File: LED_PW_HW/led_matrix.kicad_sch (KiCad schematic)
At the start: 145 parts

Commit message: imported first footprints to pcb to get an idea
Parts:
- D1, D10, D100, D101, D102, D103, D104, D105, D106, D107, D108, D109, D11, D110, D111, D112, D113, D114, D115, D116, D117, D118, D119, D12, D120, D121, D122, D123, D124, D125, D126, D127, D128, D129, D13, D130, D131, D132, D133, D134, D135, D136, D137, D138, D139, D14, D140, D141, D142, D143, D144, D15, D16, D17, D18, D19, D2, D20, D21, D22, D23, D24, D25, D26, D27, D28, D29, D3, D30, D31, D32, D33, D34, D35, D36, D37, D38, D39, D4, D40, D41, D42, D43, D44, D45, D46, D47, D48, D49, D5, D50, D51, D52, D53, D54, D55, D56, D57, D58, D59, D6, D60, D61, D62, D63, D64, D65, D66, D67, D68, D69, D7, D70, D71, D72, D73, D74, D75, D76, D77, D78, D79, D8, D80, D81, D82, D83, D84, D85, D86, D87, D88, D89, D9, D90, D91, D92, D93, D94, D95, D96, D97, D98, D99: renamed from D?; footprint (none) -> LED_SMD:LED_0201_0603Metric_Pad0.64x0.40mm_HandSolder
- U1: renamed from U?; footprint (none) -> LED_PW_HW_Library:IS31FL3732A

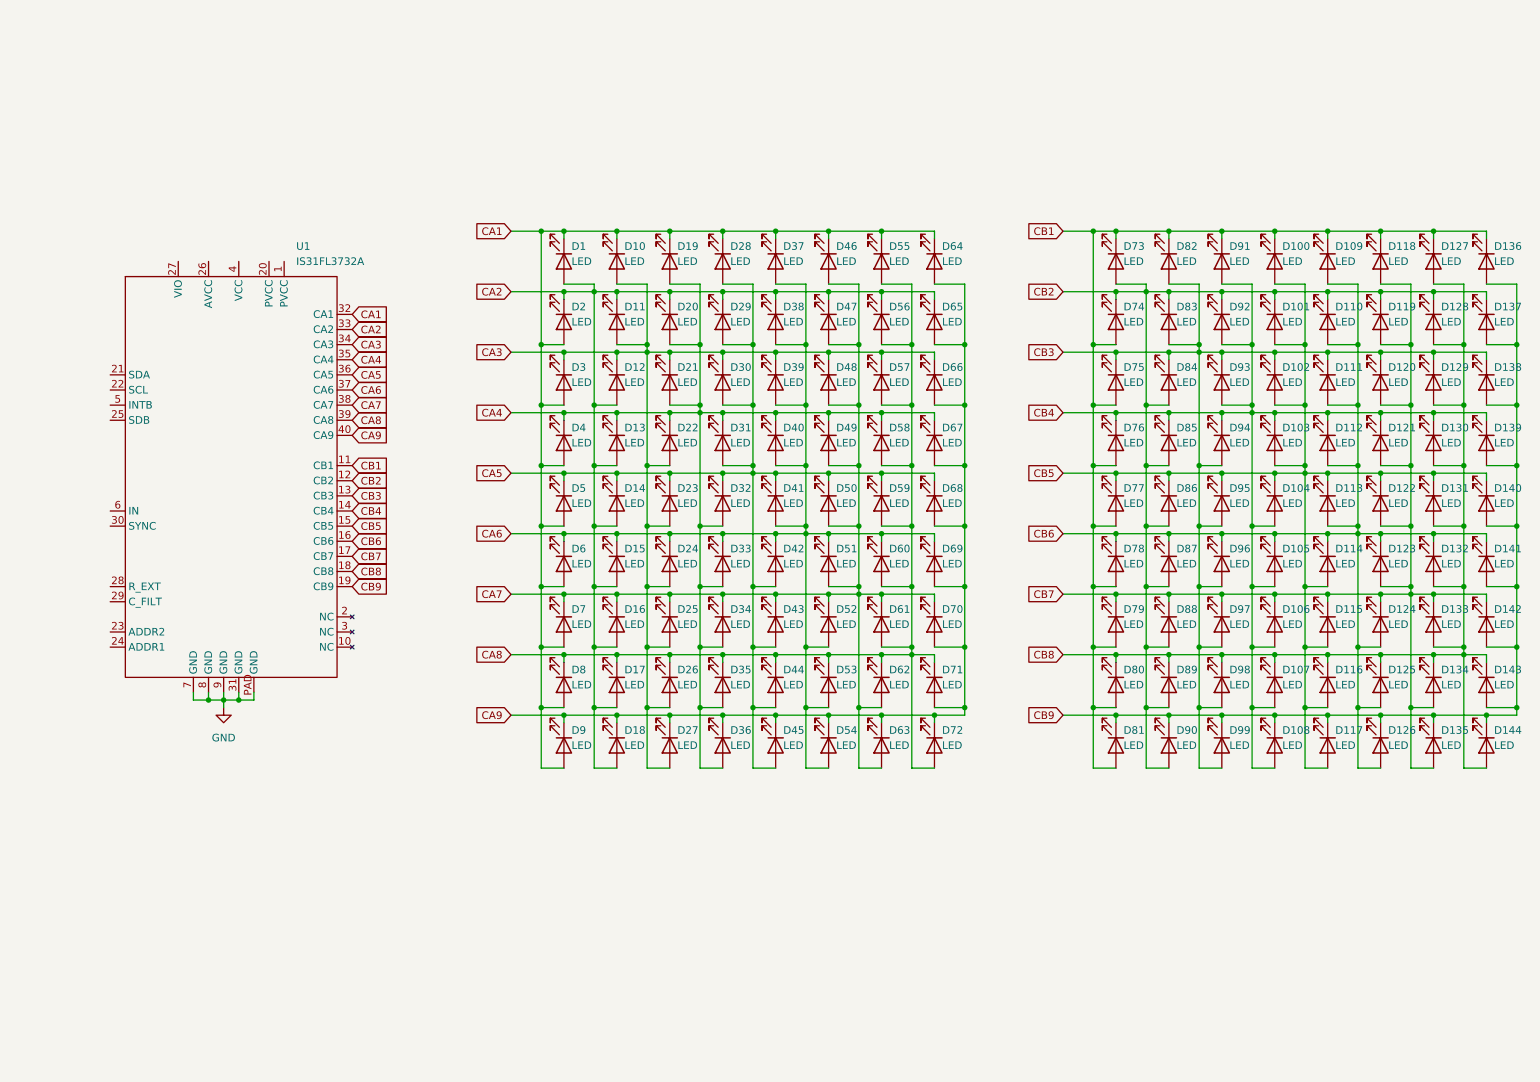
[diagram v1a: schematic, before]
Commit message: schematic of led driver part done
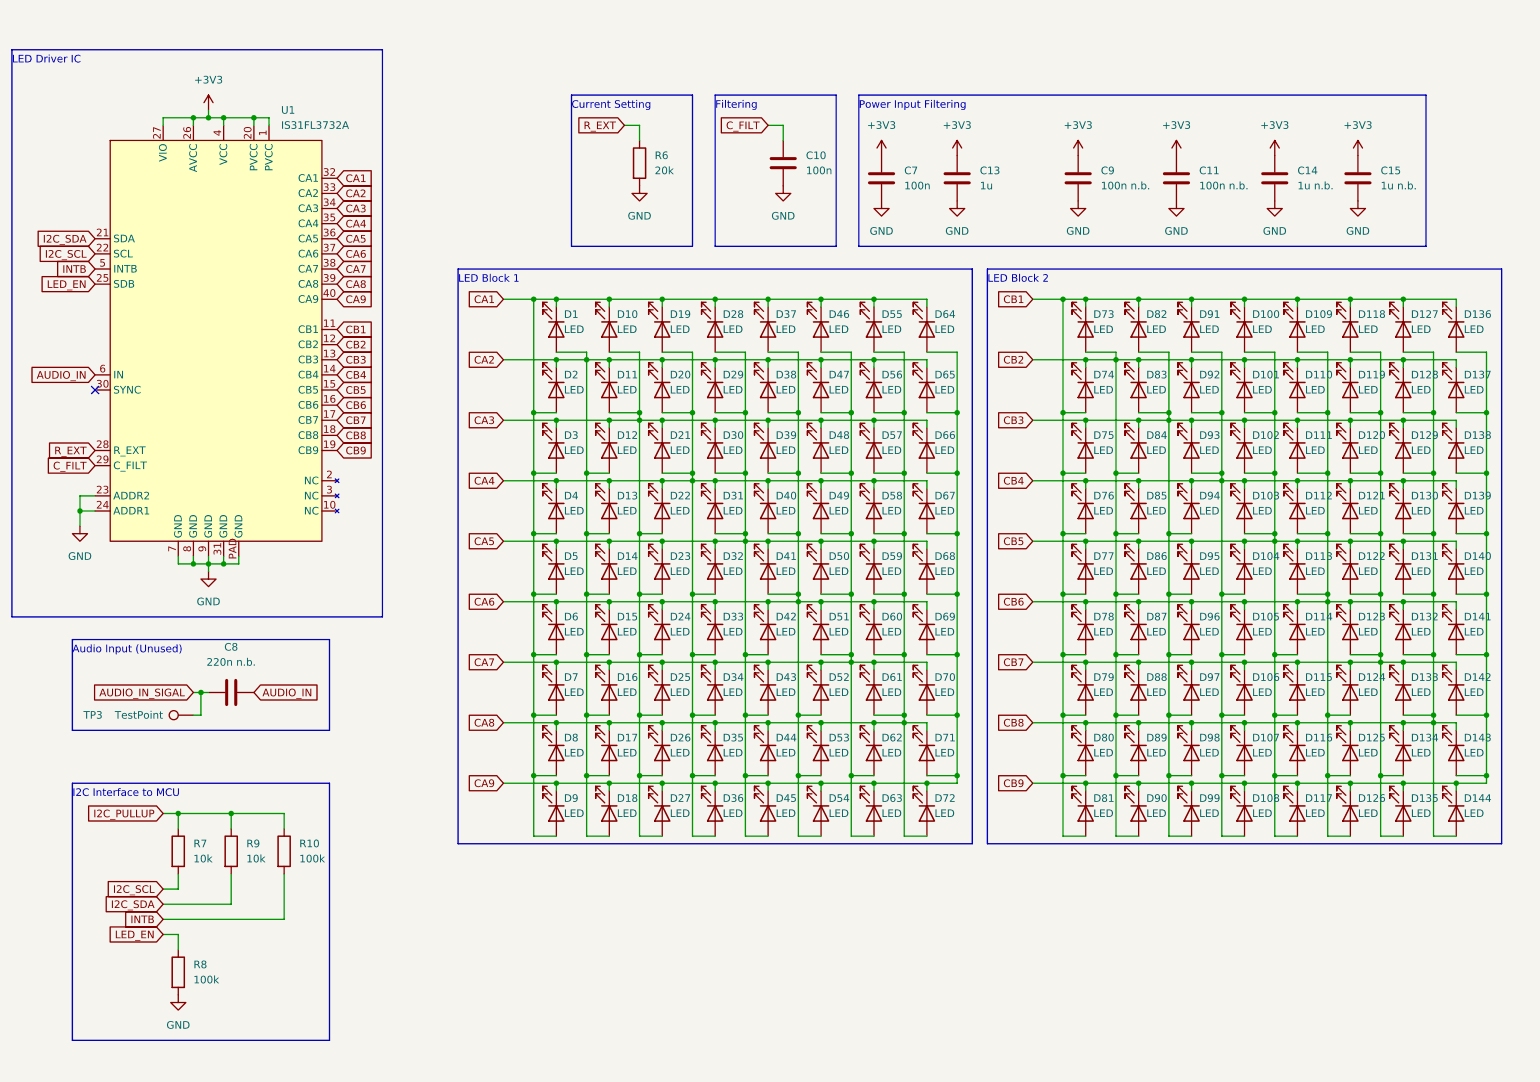
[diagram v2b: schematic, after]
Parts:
- added C10, C7: 100n, Capacitor_SMD:C_0603_1608Metric_Pad1.08x0.95mm_HandSolder, symbol Device:C
- added C11, C9: 100n n.b., Capacitor_SMD:C_0603_1608Metric_Pad1.08x0.95mm_HandSolder, symbol Device:C
- added C13: 1u, Capacitor_SMD:C_0603_1608Metric_Pad1.08x0.95mm_HandSolder, symbol Device:C
- added C14, C15: 1u n.b., Capacitor_SMD:C_0603_1608Metric_Pad1.08x0.95mm_HandSolder, symbol Device:C
- added C8: 220n n.b., Capacitor_SMD:C_0603_1608Metric_Pad1.08x0.95mm_HandSolder, symbol Device:C
- added R10, R8: 100k, Resistor_SMD:R_0603_1608Metric_Pad0.98x0.95mm_HandSolder, symbol Device:R
- added R6: 20k, Resistor_SMD:R_0603_1608Metric_Pad0.98x0.95mm_HandSolder, symbol Device:R
- added R7, R9: 10k, Resistor_SMD:R_0603_1608Metric_Pad0.98x0.95mm_HandSolder, symbol Device:R
- added TP3: TestPoint, TestPoint:TestPoint_Pad_D1.5mm, symbol Connector:TestPoint
- D1, D10, D100, D101, D102, D103, D104, D105, D106, D107, D108, D109, D11, D110, D111, D112, D113, D114, D115, D116, D117, D118, D119, D12, D120, D121, D122, D123, D124, D125, D126, D127, D128, D129, D13, D130, D131, D132, D133, D134, D135, D136, D137, D138, D139, D14, D140, D141, D142, D143, D144, D15, D16, D17, D18, D19, D2, D20, D21, D22, D23, D24, D25, D26, D27, D28, D29, D3, D30, D31, D32, D33, D34, D35, D36, D37, D38, D39, D4, D40, D41, D42, D43, D44, D45, D46, D47, D48, D49, D5, D50, D51, D52, D53, D54, D55, D56, D57, D58, D59, D6, D60, D61, D62, D63, D64, D65, D66, D67, D68, D69, D7, D70, D71, D72, D73, D74, D75, D76, D77, D78, D79, D8, D80, D81, D82, D83, D84, D85, D86, D87, D88, D89, D9, D90, D91, D92, D93, D94, D95, D96, D97, D98, D99: footprint LED_SMD:LED_0201_0603Metric_Pad0.64x0.40mm_HandSolder -> LED_SMD:LED_0603_1608Metric_Pad1.05x0.95mm_HandSolder
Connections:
- net GND: now also U1.23 (ADDR2), U1.24 (ADDR1), C10.2, C11.2, C13.2, C14.2, C15.2, C7.2, C9.2, R6.2, R8.2
- net +3V3: now reaches U1.1 (PVCC)
- net +3V3: now also U1.20 (PVCC), U1.26 (AVCC), U1.27 (VIO), U1.4 (VCC), C11.1, C13.1, C14.1, C15.1, C7.1, C9.1
- net I2C_SDA: now reaches U1.21 (SDA)
- net I2C_SDA: now also R9.2
- net I2C_SCL: now reaches U1.22 (SCL)
- net I2C_SCL: now also R7.2
- net LED_EN: now reaches U1.25 (SDB)
- net LED_EN: now also R8.1
- net R_EXT: now reaches U1.28 (R_EXT)
- net R_EXT: now also R6.1
- net C_FILT: now reaches U1.29 (C_FILT)
- net C_FILT: now also C10.1
- net INTB: now reaches U1.5 (INTB)
- net INTB: now also R10.2
- net AUDIO_IN: now reaches U1.6 (IN)
- net AUDIO_IN: now also C8.1
- new net AUDIO_IN_SIGAL: C8.2, TP3.1
- new net I2C_PULLUP: R10.1, R7.1, R9.1
- no-connect marks 0 -> 1
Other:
- note added: "Audio Input (Unused)"
- note added: "Current Setting"
- note added: "Filtering"
- note added: "I2C Interface to MCU"
- note added: "LED Block 1"
- note added: "LED Block 2"
- note added: "LED Driver IC"
- note added: "Power Input Filtering"
- moved on the sheet: D1, D10, D100, D101, D102, D103, D104, D105, D106, D107, D108, D109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

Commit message: giving up for now and going with 72 leds
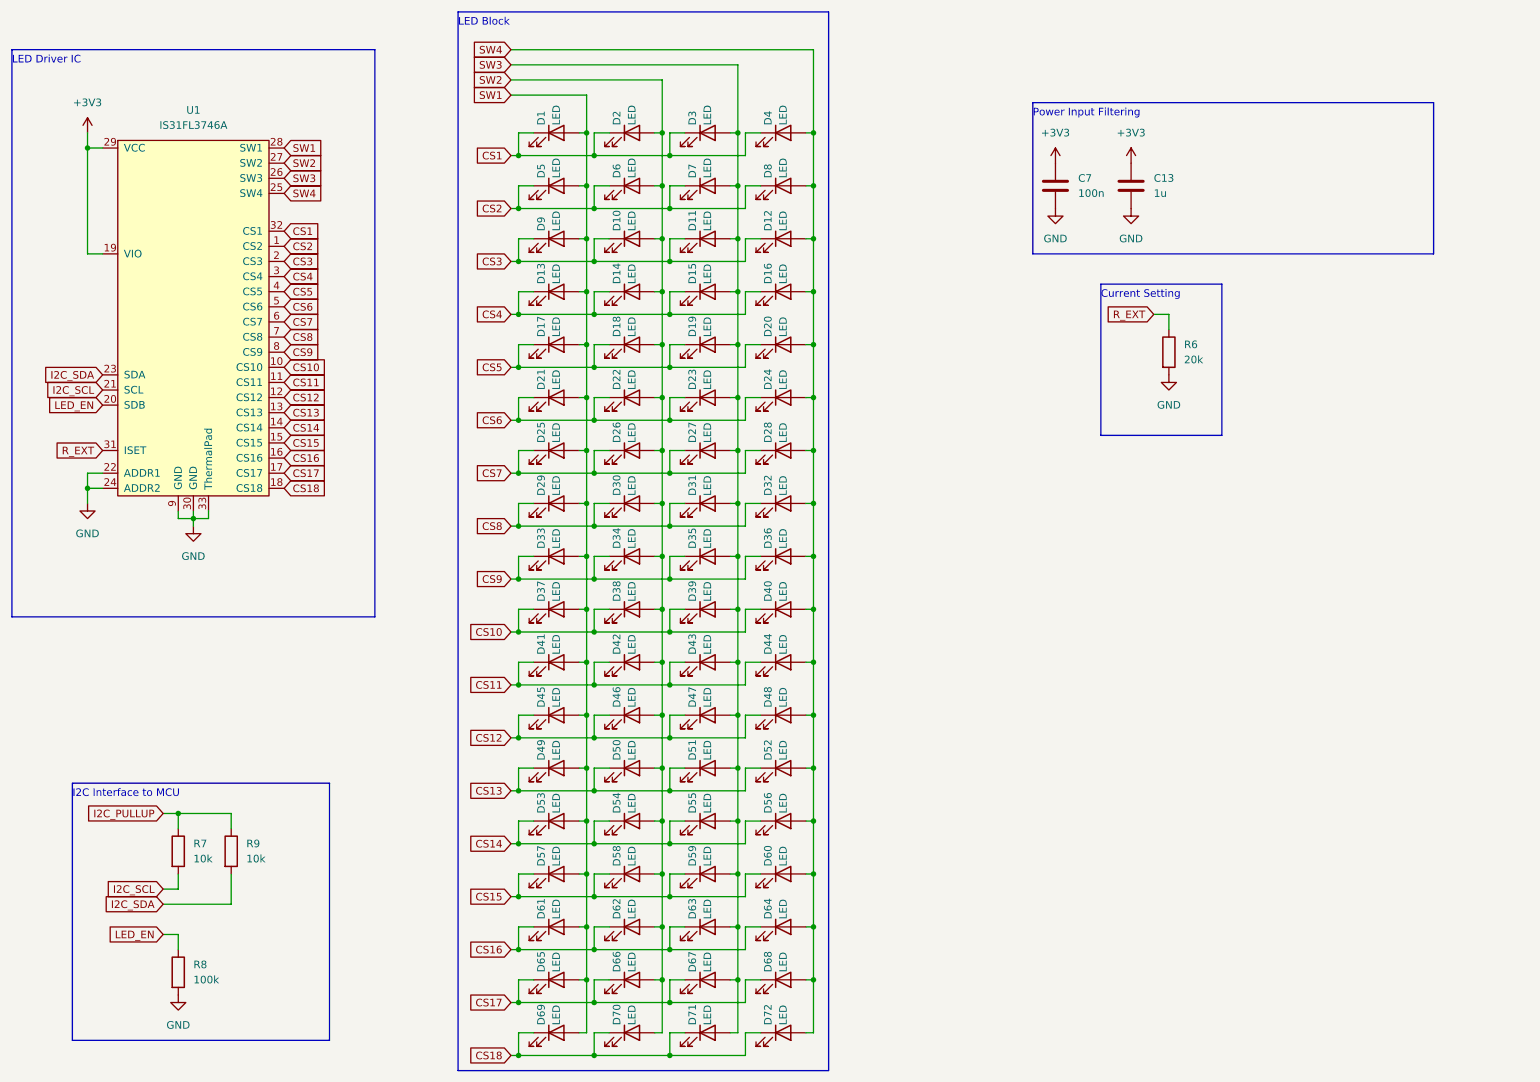
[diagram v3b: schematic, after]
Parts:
- removed C10: 100n, Capacitor_SMD:C_0603_1608Metric_Pad1.08x0.95mm_HandSolder, symbol Device:C
- removed C11, C9: 100n n.b., Capacitor_SMD:C_0603_1608Metric_Pad1.08x0.95mm_HandSolder, symbol Device:C
- removed C14, C15: 1u n.b., Capacitor_SMD:C_0603_1608Metric_Pad1.08x0.95mm_HandSolder, symbol Device:C
- removed C8: 220n n.b., Capacitor_SMD:C_0603_1608Metric_Pad1.08x0.95mm_HandSolder, symbol Device:C
- removed D100, D101, D102, D103, D104, D105, D106, D107, D108, D109, D110, D111, D112, D113, D114, D115, D116, D117, D118, D119, D120, D121, D122, D123, D124, D125, D126, D127, D128, D129, D130, D131, D132, D133, D134, D135, D136, D137, D138, D139, D140, D141, D142, D143, D144, D73, D74, D75, D76, D77, D78, D79, D80, D81, D82, D83, D84, D85, D86, D87, D88, D89, D90, D91, D92, D93, D94, D95, D96, D97, D98, D99: LED, LED_SMD:LED_0603_1608Metric_Pad1.05x0.95mm_HandSolder, symbol Device:LED
- removed R10: 100k, Resistor_SMD:R_0603_1608Metric_Pad0.98x0.95mm_HandSolder, symbol Device:R
- removed TP3: TestPoint, TestPoint:TestPoint_Pad_D1.5mm, symbol Connector:TestPoint
- removed U1: IS31FL3732A, LED_PW_HW_Library:IS31FL3732A, symbol LED_PW_HW_Library:IS31FL3732A
- added U1: IS31FL3746A, LED_Clock_HW:QFN-32_EP_4x4_Pitch0.4mm, symbol LED_Clock_HW:IS31FL3746A
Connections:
- net +3V3: now also U1.19 (VIO), U1.29 (VCC)
- net GND: now also U1.22 (ADDR1), U1.24 (ADDR2), U1.30 (GND), U1.33 (ThermalPad), U1.9 (GND)
- net I2C_SCL: now also U1.21 (SCL)
- net I2C_SDA: now also U1.23 (SDA)
- net LED_EN: now also U1.20 (SDB)
- net R_EXT: now also U1.31 (ISET)
- removed net CA1: D1.1 (K), D10.1 (K), D19.1 (K), D2.2 (A), D28.1 (K), D3.2 (A), D37.1 (K), D4.2 (A), D46.1 (K), D5.2 (A), D55.1 (K), D6.2 (A), D64.1 (K), D7.2 (A), D8.2 (A), D9.2 (A)
- removed net CA2: D1.2 (A), D11.1 (K), D12.2 (A), D13.2 (A), D14.2 (A), D15.2 (A), D16.2 (A), D17.2 (A), D18.2 (A), D2.1 (K), D20.1 (K), D29.1 (K), D38.1 (K), D47.1 (K), D56.1 (K), D65.1 (K)
- removed net CA3: D10.2 (A), D11.2 (A), D12.1 (K), D21.1 (K), D22.2 (A), D23.2 (A), D24.2 (A), D25.2 (A), D26.2 (A), D27.2 (A), D3.1 (K), D30.1 (K), D39.1 (K), D48.1 (K), D57.1 (K), D66.1 (K)
- removed net CA4: D13.1 (K), D19.2 (A), D20.2 (A), D21.2 (A), D22.1 (K), D31.1 (K), D32.2 (A), D33.2 (A), D34.2 (A), D35.2 (A), D36.2 (A), D4.1 (K), D40.1 (K), D49.1 (K), D58.1 (K), D67.1 (K)
- removed net CA5: D14.1 (K), D23.1 (K), D28.2 (A), D29.2 (A), D30.2 (A), D31.2 (A), D32.1 (K), D41.1 (K), D42.2 (A), D43.2 (A), D44.2 (A), D45.2 (A), D5.1 (K), D50.1 (K), D59.1 (K), D68.1 (K)
- removed net CA6: D15.1 (K), D24.1 (K), D33.1 (K), D37.2 (A), D38.2 (A), D39.2 (A), D40.2 (A), D41.2 (A), D42.1 (K), D51.1 (K), D52.2 (A), D53.2 (A), D54.2 (A), D6.1 (K), D60.1 (K), D69.1 (K)
- removed net CA7: D16.1 (K), D25.1 (K), D34.1 (K), D43.1 (K), D46.2 (A), D47.2 (A), D48.2 (A), D49.2 (A), D50.2 (A), D51.2 (A), D52.1 (K), D61.1 (K), D62.2 (A), D63.2 (A), D7.1 (K), D70.1 (K)
- removed net CA8: D17.1 (K), D26.1 (K), D35.1 (K), D44.1 (K), D53.1 (K), D55.2 (A), D56.2 (A), D57.2 (A), D58.2 (A), D59.2 (A), D60.2 (A), D61.2 (A), D62.1 (K), D71.1 (K), D72.2 (A), D8.1 (K)
- removed net CA9: D18.1 (K), D27.1 (K), D36.1 (K), D45.1 (K), D54.1 (K), D63.1 (K), D64.2 (A), D65.2 (A), D66.2 (A), D67.2 (A), D68.2 (A), D69.2 (A), D70.2 (A), D71.2 (A), D72.1 (K), D9.1 (K)
- new net CS1: D1.1 (K), D2.1 (K), D3.1 (K), D4.1 (K), U1.32 (CS1)
- new net CS10: D37.1 (K), D38.1 (K), D39.1 (K), D40.1 (K), U1.10 (CS10)
- new net CS11: D41.1 (K), D42.1 (K), D43.1 (K), D44.1 (K), U1.11 (CS11)
- new net CS12: D45.1 (K), D46.1 (K), D47.1 (K), D48.1 (K), U1.12 (CS12)
- new net CS13: D49.1 (K), D50.1 (K), D51.1 (K), D52.1 (K), U1.13 (CS13)
- new net CS14: D53.1 (K), D54.1 (K), D55.1 (K), D56.1 (K), U1.14 (CS14)
- new net CS15: D57.1 (K), D58.1 (K), D59.1 (K), D60.1 (K), U1.15 (CS15)
- new net CS16: D61.1 (K), D62.1 (K), D63.1 (K), D64.1 (K), U1.16 (CS16)
- new net CS17: D65.1 (K), D66.1 (K), D67.1 (K), D68.1 (K), U1.17 (CS17)
- new net CS18: D69.1 (K), D70.1 (K), D71.1 (K), D72.1 (K), U1.18 (CS18)
- new net CS2: D5.1 (K), D6.1 (K), D7.1 (K), D8.1 (K), U1.1 (CS2)
- new net CS3: D10.1 (K), D11.1 (K), D12.1 (K), D9.1 (K), U1.2 (CS3)
- new net CS4: D13.1 (K), D14.1 (K), D15.1 (K), D16.1 (K), U1.3 (CS4)
- new net CS5: D17.1 (K), D18.1 (K), D19.1 (K), D20.1 (K), U1.4 (CS5)
- new net CS6: D21.1 (K), D22.1 (K), D23.1 (K), D24.1 (K), U1.5 (CS6)
- new net CS7: D25.1 (K), D26.1 (K), D27.1 (K), D28.1 (K), U1.6 (CS7)
- new net CS8: D29.1 (K), D30.1 (K), D31.1 (K), D32.1 (K), U1.7 (CS8)
- new net CS9: D33.1 (K), D34.1 (K), D35.1 (K), D36.1 (K), U1.8 (CS9)
- new net SW1: D1.2 (A), D13.2 (A), D17.2 (A), D21.2 (A), D25.2 (A), D29.2 (A), D33.2 (A), D37.2 (A), D41.2 (A), D45.2 (A), D49.2 (A), D5.2 (A), D53.2 (A), D57.2 (A), D61.2 (A), D65.2 (A), D69.2 (A), D9.2 (A), U1.28 (SW1)
- new net SW2: D10.2 (A), D14.2 (A), D18.2 (A), D2.2 (A), D22.2 (A), D26.2 (A), D30.2 (A), D34.2 (A), D38.2 (A), D42.2 (A), D46.2 (A), D50.2 (A), D54.2 (A), D58.2 (A), D6.2 (A), D62.2 (A), D66.2 (A), D70.2 (A), U1.27 (SW2)
- new net SW3: D11.2 (A), D15.2 (A), D19.2 (A), D23.2 (A), D27.2 (A), D3.2 (A), D31.2 (A), D35.2 (A), D39.2 (A), D43.2 (A), D47.2 (A), D51.2 (A), D55.2 (A), D59.2 (A), D63.2 (A), D67.2 (A), D7.2 (A), D71.2 (A), U1.26 (SW3)
- new net SW4: D12.2 (A), D16.2 (A), D20.2 (A), D24.2 (A), D28.2 (A), D32.2 (A), D36.2 (A), D4.2 (A), D40.2 (A), D44.2 (A), D48.2 (A), D52.2 (A), D56.2 (A), D60.2 (A), D64.2 (A), D68.2 (A), D72.2 (A), D8.2 (A), U1.25 (SW4)
- no-connect marks 1 -> 0
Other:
- note added: "LED Block"
- note removed: "Audio Input (Unused)"
- note removed: "Filtering"
- note removed: "LED Block 1"
- note removed: "LED Block 2"
- moved on the sheet: C13, C7, D1, R6
